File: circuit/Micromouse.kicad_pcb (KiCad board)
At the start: 2 copper layers, 0 parts

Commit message: スーパーエンジニアの登竜門たる文彦は当然スーパーエンジニア
あってぃ許さない
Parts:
- added C1: 4.7u, Capacitor_SMD:C_0805_2012Metric, F.Cu at (109.2, 58.4)
- added C10: 0.1u, Capacitor_SMD:C_0603_1608Metric, F.Cu at (102.6, 51.0)
- added C11: 0.1u, Capacitor_SMD:C_0603_1608Metric, F.Cu at (115.8, 38.6)
- added C12: 0.1u, Capacitor_SMD:C_0603_1608Metric, F.Cu at (106.6, 48.4)
- added C13: 0.1u, Capacitor_SMD:C_0603_1608Metric, F.Cu at (113.3, 41.3)
- added C14: 0.1u, Capacitor_SMD:C_0603_1608Metric, F.Cu at (119.8, 34.0)
- added C15: 1u, Capacitor_SMD:C_0603_1608Metric, F.Cu at (106.6, 51.0)
- added C17: 10u, Capacitor_SMD:C_0805_2012Metric, F.Cu at (44.0, 77.7)
- added C18: 47u, Capacitor_SMD:CP_Elec_6.3x7.7, F.Cu at (62.1, 72.9)
- added C19: 10u, Capacitor_SMD:C_0805_2012Metric, F.Cu at (39.5, 77.7)
- added C2: 0.1uF, Capacitor_SMD:C_0603_1608Metric, F.Cu at (87.6, 72.5)
- added C20: 10u, Capacitor_SMD:C_0805_2012Metric, F.Cu at (35.1, 77.7)
- added C21: 10u, Capacitor_SMD:C_0603_1608Metric, F.Cu at (72.4, 44.0)
- added C22: 10u, Capacitor_SMD:C_0603_1608Metric, F.Cu at (63.3, 51.5)
- added C23: 2.2u, Capacitor_SMD:C_0603_1608Metric, F.Cu at (110.6, 46.3)
- added C24: 2.2u, Capacitor_SMD:C_0603_1608Metric, F.Cu at (106.2, 70.1)
- added C3: 1u, Capacitor_SMD:C_0603_1608Metric, F.Cu at (102.2, 70.1)
- added C4: 2.2u, Capacitor_SMD:C_0603_1608Metric, F.Cu at (106.6, 67.2)
- added C5: 0.1u, Capacitor_SMD:C_0603_1608Metric, F.Cu at (119.8, 36.5)
- added C6: 2.2u, Capacitor_SMD:C_0603_1608Metric, F.Cu at (113.3, 43.8)
- added C7: 0.1u, Capacitor_SMD:C_0603_1608Metric, F.Cu at (83.5, 52.6)
- added C8: 0.1u, Capacitor_SMD:C_0603_1608Metric, F.Cu at (109.3, 43.6)
- added C9: 4.7u, Capacitor_SMD:C_0603_1608Metric, F.Cu at (115.8, 36.1)
- added CN1: Battery, Connector_JST:JST_PH_B2B-PH-K_1x02_P2.00mm_Vertical, F.Cu at (96.6, 59.6)
- added CN2: Battery, Connector_JST:JST_PH_B2B-PH-K_1x02_P2.00mm_Vertical, F.Cu at (95.2, 67.7)
- added D1: PWR_LED(Red), LED_SMD:LED_0603_1608Metric, F.Cu at (83.5, 72.5)
- added D2: TICK_LED, LED_SMD:LED_0603_1608Metric, F.Cu at (118.5, 31.4)
- added D3: DBG_LED0, LED_SMD:LED_0603_1608Metric, F.Cu at (111.8, 36.2)
- added D4: DBG_LED1, LED_SMD:LED_0603_1608Metric, F.Cu at (111.8, 38.8)
- added D5: DBG_LED2, LED_SMD:LED_0603_1608Metric, F.Cu at (102.6, 48.4)
- added D6: SFH4550, LED_THT:LED_D5.0mm_Horizontal_O3.81mm_Z9.0mm, F.Cu at (35.4, 31.9)
- added D7: SFH4550, LED_THT:LED_D5.0mm_Horizontal_O3.81mm_Z9.0mm, F.Cu at (42.9, 31.9)
- added D8: SFH4550, LED_THT:LED_D5.0mm_Horizontal_O3.81mm_Z9.0mm, F.Cu at (50.4, 31.9)
- added D9: SFH4550, LED_THT:LED_D5.0mm_Horizontal_O3.81mm_Z9.0mm, F.Cu at (57.9, 31.9)
- added J1: DBG_CN, Connector_PinSocket_2.54mm:PinSocket_1x03_P2.54mm_Vertical, F.Cu at (98.3, 44.7)
- added J2: ICM-20602_1-4pin, Connector_PinSocket_2.54mm:PinSocket_1x04_P2.54mm_Vertical, F.Cu at (102.9, 32.5)
- added J3: TEST_1P, TestPoint:TestPoint_Pad_D1.0mm, F.Cu at (114.2, 49.3)
- added J4: ICM-20602_5-8pin, Connector_PinSocket_2.54mm:PinSocket_1x04_P2.54mm_Vertical, F.Cu at (107.5, 32.5)
- added J5: TEST_1P, TestPoint:TestPoint_Pad_D1.0mm, F.Cu at (120.9, 41.8)
- added J6: Conn_01x04, Connector_PinSocket_2.54mm:PinSocket_1x04_P2.54mm_Vertical, F.Cu at (98.3, 32.5)
- added J7: Conn_02x03_Odd_Even, Connector_IDC:IDC-Header_2x03_P2.54mm_Vertical, F.Cu at (50.1, 64.9)
- added J8: Conn_02x03_Odd_Even, Connector_IDC:IDC-Header_2x03_P2.54mm_Vertical, F.Cu at (38.1, 64.9)
- added LS1: CSS-0575A-SMT, Original:CUI_CSS-0575A-SMT, F.Cu at (85.2, 48.0)
- added Q1: IRLML6402, Package_TO_SOT_SMD:SOT-23, F.Cu at (103.8, 63.6)
- added Q2: IRLML6344, Package_TO_SOT_SMD:SOT-23, F.Cu at (91.2, 51.6)
- added Q3: ST-1KL3A, LED_THT:LED_D5.0mm, F.Cu at (65.3, 41.5)
- added Q5: ST-1KL3A, LED_THT:LED_D5.0mm, F.Cu at (72.8, 33.9)
- added Q7: ST-1KL3A, LED_THT:LED_D5.0mm, F.Cu at (52.2, 49.0)
- added Q9: ST-1KL3A, LED_THT:LED_D5.0mm, F.Cu at (65.3, 33.9)
- added R1: 100k 0.25W, Resistor_SMD:R_0603_1608Metric, F.Cu at (108.1, 64.1)
- added R10: 10k, Resistor_SMD:R_0603_1608Metric, F.Cu at (119.8, 39.0)
- added R11: 10k, Resistor_SMD:R_0603_1608Metric, F.Cu at (34.9, 52.9)
- added R12: 1k, Resistor_SMD:R_0603_1608Metric, F.Cu at (38.9, 52.9)
- added R13: 10 1/10W, Resistor_SMD:R_0603_1608Metric, F.Cu at (42.9, 52.9)
- added R14: 24k, Resistor_SMD:R_0603_1608Metric, F.Cu at (46.9, 54.0)
- added R15: 1k, Resistor_SMD:R_0603_1608Metric, F.Cu at (59.3, 46.4)
- added R16: 10 1/10W, Resistor_SMD:R_0603_1608Metric, F.Cu at (50.9, 54.0)
- added R17: 1k, Resistor_SMD:R_0603_1608Metric, F.Cu at (72.4, 38.9)
- added R18: 24k, Resistor_SMD:R_0603_1608Metric, F.Cu at (54.9, 54.0)
- added R19: 10k, Resistor_SMD:R_0603_1608Metric, F.Cu at (59.3, 49.0)
- added R2: 20k, Resistor_SMD:R_0805_2012Metric, F.Cu at (102.4, 67.4)
- added R20: 1k, Resistor_SMD:R_0603_1608Metric, F.Cu at (59.3, 51.5)
- added R21: 24k, Resistor_SMD:R_0603_1608Metric, F.Cu at (63.3, 46.5)
- added R22: 10k, Resistor_SMD:R_0603_1608Metric, F.Cu at (72.4, 41.5)
- added R23: 10 1/10W, Resistor_SMD:R_0603_1608Metric, F.Cu at (67.3, 46.5)
- added R24: 10 1/10W, Resistor_SMD:R_0603_1608Metric, F.Cu at (63.3, 49.0)
- added R25: 24k, Resistor_SMD:R_0603_1608Metric, F.Cu at (59.3, 54.0)
- added R26: 10k, Resistor_SMD:R_0603_1608Metric, F.Cu at (76.4, 38.9)
- added R3: 10k, Resistor_SMD:R_0805_2012Metric, F.Cu at (109.2, 61.4)
- added R4: 1k, Resistor_SMD:R_0603_1608Metric, F.Cu at (102.2, 72.6)
- added R5: 10k, Resistor_SMD:R_0603_1608Metric, F.Cu at (114.6, 46.5)
- added R6: 10k, Resistor_SMD:R_0603_1608Metric, F.Cu at (110.6, 51.4)
- added R7: 10, Resistor_SMD:R_0603_1608Metric, F.Cu at (117.3, 44.0)
- added R8: 10k, Resistor_SMD:R_0603_1608Metric, F.Cu at (117.3, 41.5)
- added R9: 10k, Resistor_SMD:R_0603_1608Metric, F.Cu at (110.6, 48.9)
- added SW1: SW_SPDT, Button_Switch_THT:SW_CuK_JS202011CQN_DPDT_Straight, F.Cu at (84.5, 66.4)
- added SW2: SW_Push, Original:SW_TACT_ALPS_SKRPABE010, F.Cu at (113.1, 32.5)
- added SW3: SW_Push, Original:SW_TACT_ALPS_SKRPABE010, F.Cu at (92.3, 47.0)
- added SW4: SW_Push, Original:SW_TACT_ALPS_SKRPABE010, F.Cu at (103.9, 44.8)
- added U1: NJM7805S, Package_TO_SOT_SMD:TO-252-2, F.Cu at (87.6, 60.9)
- added U2: TB6612FNG, Package_SO:SSOP-24_5.3x8.2mm_P0.65mm, F.Cu at (62.1, 63.8)
- added U3: STM32F405RGTx, Package_QFP:LQFP-64_10x10mm_P0.5mm, F.Cu at (88.7, 37.4)
- added U4: ADP7182AUJZ-3.3, Package_TO_SOT_SMD:TSOT-23-5, F.Cu at (104.3, 59.1)
- added U5: AD8397, Package_SO:SOIC-8_3.9x4.9mm_P1.27mm, F.Cu at (37.1, 48.4)
- added U6: AD8397, Package_SO:SOIC-8_3.9x4.9mm_P1.27mm, F.Cu at (45.5, 48.4)
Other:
- board outline added: 268.6 x 181.3 mm

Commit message: AW何も分からん
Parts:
- removed J2: ICM-20602_1-4pin, Connector_PinSocket_2.54mm:PinSocket_1x04_P2.54mm_Vertical
- removed J4: ICM-20602_5-8pin, Connector_PinSocket_2.54mm:PinSocket_1x04_P2.54mm_Vertical
- removed J6: Conn_01x04, Connector_PinSocket_2.54mm:PinSocket_1x04_P2.54mm_Vertical
- removed the SW1 at (84.5, 66.4)
- removed SW2, SW3, SW4: SW_Push, Original:SW_TACT_ALPS_SKRPABE010
- added ICM-20602: ICM-20602-module, Original:ICM-20602, F.Cu at (190.0, 68.0)
- added RESET: SW_Push, Original:SW_TACT_ALPS_SKRPABE010, F.Cu at (154.5, 93.0)
- added SW0: SW_Push, Original:SW_TACT_ALPS_SKRPABE010, F.Cu at (205.0, 141.5)
- added SW1: SW_Push, Original:SW_TACT_ALPS_SKRPABE010, F.Cu at (209.5, 141.5)
- added SW1: SW_SPDT, Button_Switch_THT:SW_CuK_JS202011CQN_DPDT_Straight, F.Cu at (219.5, 93.5)
- added SWD: Conn_01x04, Connector_PinSocket_2.54mm:PinSocket_1x04_P2.54mm_Vertical, F.Cu at (153.0, 97.5)
- D8, D9: footprint LED_THT:LED_D5.0mm_Horizontal_O3.81mm_Z9.0mm -> Original:LED_D5.0mm_Horizontal_O3.81mm_Z9.0mm_reverse
- Q3, Q5, Q7, Q9: footprint LED_THT:LED_D5.0mm -> Original:ST-1KL3A_ForWall
- moved D6 199.7 mm to (227.0, 88.0), turned to 180 degrees
- moved J8 195.7 mm to (218.3, 141.3), turned to 90 degrees
- moved U5 171.0 mm to (207.0, 68.0), turned to 180 degrees
- moved Q3 167.6 mm to (227.0, 85.6), turned to 180 degrees
- moved D7 164.1 mm to (204.5, 60.4), turned to 105 degrees
- moved C18 144.5 mm to (190.0, 140.0)
- moved U2 143.1 mm to (190.0, 128.0), turned to 90 degrees
- moved Q5 136.3 mm to (206.7, 59.8), turned to 105 degrees
- moved J7 131.1 mm to (156.6, 141.3), turned to 90 degrees
- moved U6 128.9 mm to (173.0, 68.0), turned to 180 degrees
- moved D8 128.4 mm to (175.5, 60.4), turned to 255 degrees
- moved J1 122.5 mm to (171.5, 143.0), turned to 90 degrees
- moved Q7 121.5 mm to (173.3, 59.8), turned to 255 degrees
- moved CN2 121.2 mm to (212.0, 100.0), turned to 270 degrees
- moved CN1 120.1 mm to (212.0, 93.0), turned to 270 degrees
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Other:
- board size 268.6 x 181.3 mm -> 78 x 100 mm
- board text added: "G"
- board text added: "GND"
- board text added: "NRST"
- board text added: "RX"
- board text added: "SWCLK"
- board text added: "SWDIO"
- board text added: "TX"
- board text added: "→"

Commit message: ぽんぽんぺいん
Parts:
- moved D3 137.4 mm to (198.2, 143.0), turned to 90 degrees
- moved D5 137.1 mm to (201.9, 143.0), turned to 90 degrees
- moved D4 136.5 mm to (200.0, 143.0), turned to 90 degrees
- moved D1 134.1 mm to (215.7, 95.5), turned to 90 degrees
- moved D2 77.9 mm to (164.0, 94.7), turned to 90 degrees
- moved J1 0.12 mm to (171.4, 142.9)
- renumbered SWD to J6, RESET to SW2, SW0 to SW3, SW1 to SW4, ICM-20602 to U7
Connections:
- D2 pad 1: Net-(D2-Pad1) -> GND
- D2 pad 2: /TICK_LED -> Net-(D2-Pad2)
- D3 pad 1: Net-(D3-Pad1) -> GND
- D3 pad 2: /DBG_LED0 -> Net-(D3-Pad2)
- D4 pad 1: Net-(D4-Pad1) -> GND
- D4 pad 2: /DBG_LED1 -> Net-(D4-Pad2)
- D5 pad 1: Net-(D5-Pad1) -> GND
- D5 pad 2: /DBG_LED2 -> Net-(D5-Pad2)
- R10 pad 1: Net-(D5-Pad1) -> /DBG_LED2
- R10 pad 2: GND -> Net-(D5-Pad2)
- R5 pad 1: Net-(D2-Pad1) -> /TICK_LED
- R5 pad 2: GND -> Net-(D2-Pad2)
- R6 pad 1: Net-(D3-Pad1) -> /DBG_LED0
- R6 pad 2: GND -> Net-(D3-Pad2)
- R9 pad 1: Net-(D4-Pad1) -> /DBG_LED1
- R9 pad 2: GND -> Net-(D4-Pad2)

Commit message: 何となーくの部品配置
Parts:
- moved R12 139.9 mm to (175.6, 82.4), turned to 90 degrees
- moved R11 132.4 mm to (166.8, 64.3), turned to 90 degrees
- moved R13 128.7 mm to (170.6, 68.7), turned to 270 degrees
- moved R14 122.4 mm to (168.7, 66.0), turned to 90 degrees
- moved C20 120.9 mm to (153.0, 104.3)
- moved C19 116.0 mm to (153.2, 100.8)
- moved R16 111.2 mm to (161.8, 61.9)
- moved C17 106.6 mm to (143.5, 115.8), turned to 180 degrees
- moved C8 106.2 mm to (164.7, 134.2), turned to 180 degrees
- moved C5 105.7 mm to (160.0, 134.3), turned to 180 degrees
- moved R10 104.5 mm to (156.6, 136.8), turned to 270 degrees
- moved C21 103.9 mm to (152.6, 110.0)
- moved R18 101.6 mm to (156.1, 63.8)
- moved R9 98.4 mm to (154.7, 136.8), turned to 270 degrees
- moved R19 98.4 mm to (156.1, 66.3), turned to 270 degrees
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- renumbered D3 to LED0, D4 to LED1, D5 to LED2

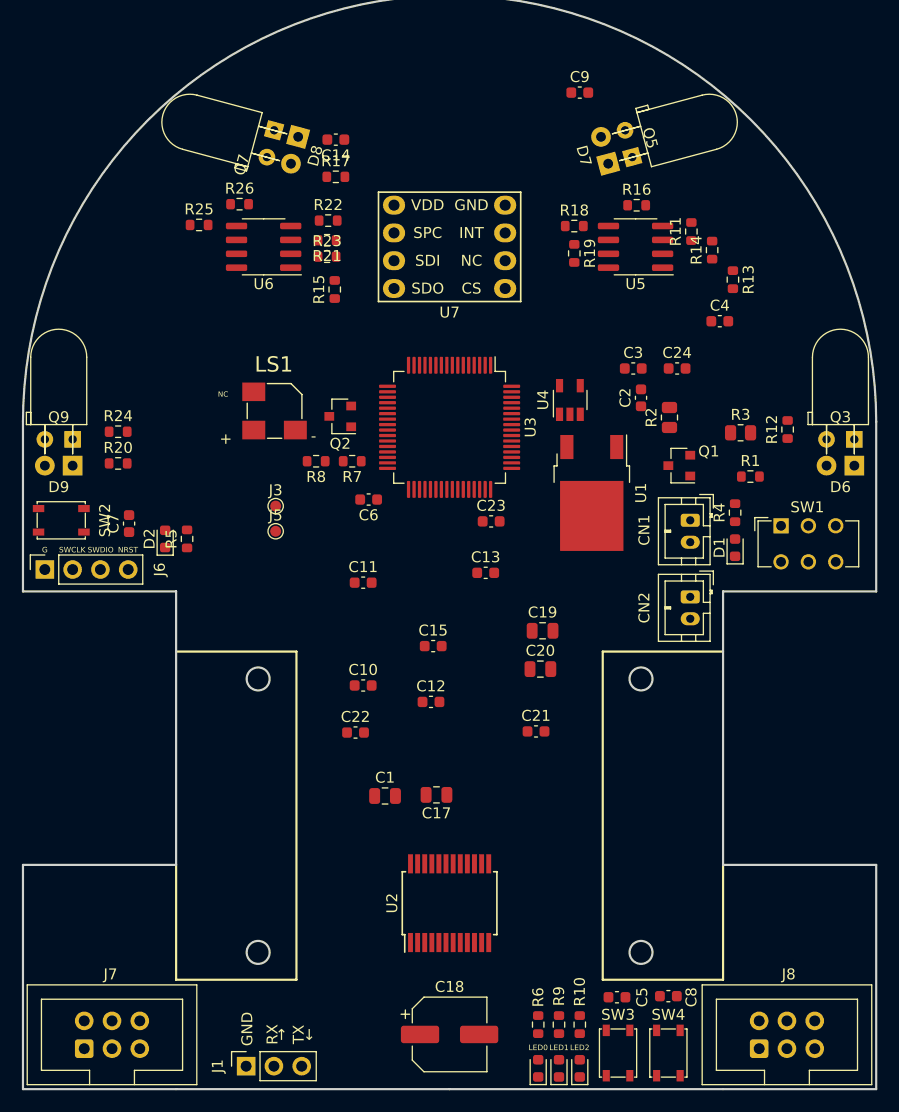
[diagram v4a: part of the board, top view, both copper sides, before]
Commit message: 配置大体完了．配線分からん
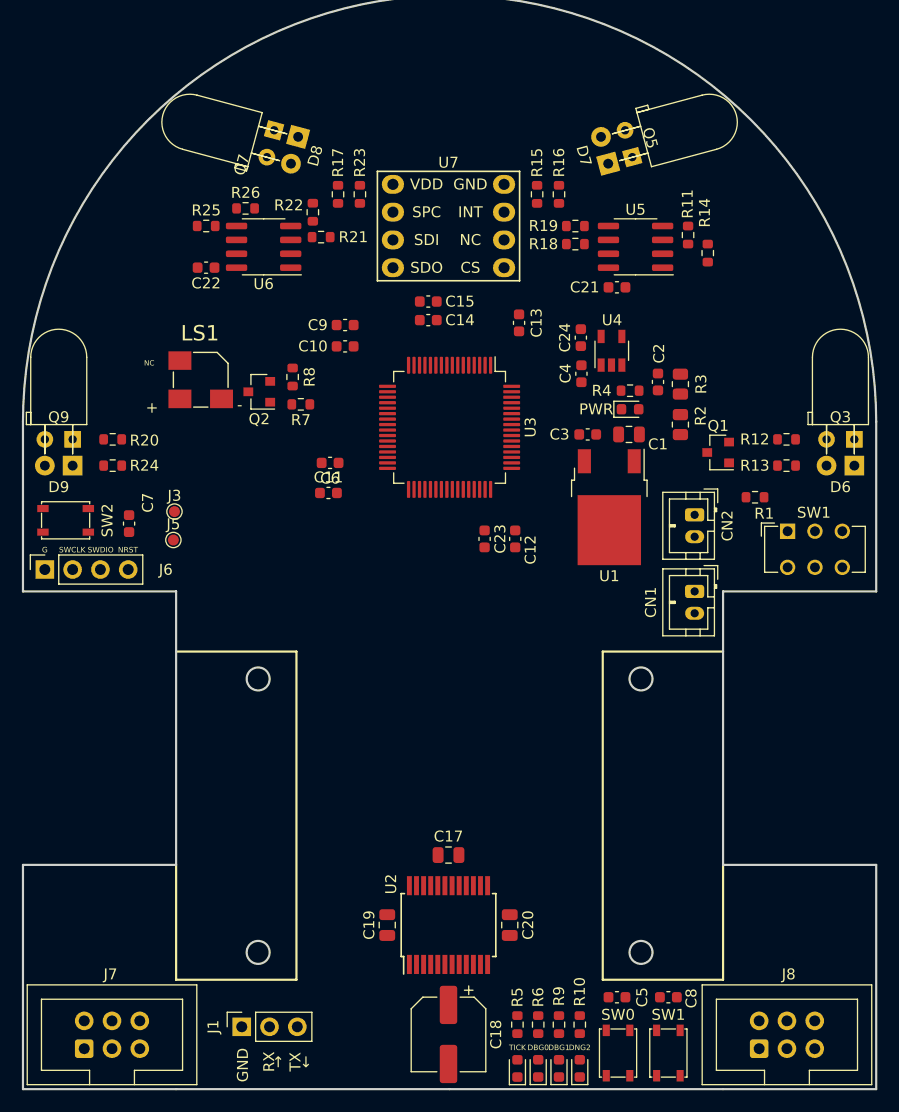
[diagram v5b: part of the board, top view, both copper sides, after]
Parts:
- removed D1: PWR_LED(Red), LED_SMD:LED_0603_1608Metric
- removed D2: TICK_LED, LED_SMD:LED_0603_1608Metric
- added PWR: PWR_LED(Red), LED_SMD:LED_0603_1608Metric, F.Cu at (161.2, 80.5)
- added TICK: TICK_LED, LED_SMD:LED_0603_1608Metric, F.Cu at (150.9, 140.8)
- moved R5 53.7 mm to (150.9, 136.8), turned to 270 degrees
- moved C22 44.6 mm to (122.4, 67.6), turned to 180 degrees
- moved C21 41.3 mm to (160.0, 69.4)
- moved C1 39.9 mm to (161.1, 82.8), turned to 180 degrees
- moved C15 31.5 mm to (142.8, 70.7), turned to 180 degrees
- moved C10 31.0 mm to (135.2, 74.8), turned to 180 degrees
- moved C19 30.4 mm to (139.0, 127.7), turned to 270 degrees
- moved C9 30.2 mm to (135.2, 72.8), turned to 180 degrees
- moved C20 23.6 mm to (150.2, 127.7), turned to 270 degrees
- moved C13 23.1 mm to (151.1, 72.7), turned to 90 degrees
- moved R15 20.4 mm to (152.7, 60.9), turned to 270 degrees
- moved C14 18.5 mm to (142.8, 72.4)
- moved R13 17.7 mm to (175.5, 85.7), turned to 180 degrees
- moved C12 16.8 mm to (150.7, 92.4), turned to 270 degrees
- moved R4 14.7 mm to (161.2, 78.8), turned to 0 degrees
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- renumbered LED0 to DBG0, LED1 to DBG1, LED2 to DNG2, SW3 to SW0, SW4 to SW1

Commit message: 1A＝1ｍｍ・・・結構大変
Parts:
- moved R3 1.78 mm to (166.2, 80.0)
- moved C2 1.77 mm to (164.2, 79.8)
- moved R2 1.68 mm to (166.2, 83.6)
- moved C18 1.27 mm to (144.6, 139.0), turned to 0 degrees
- moved R1 1.12 mm to (173.4, 89.4)
- moved CN1 0.72 mm to (166.4, 97.3)
- moved CN2 0.70 mm to (166.4, 90.2)
- moved U4 0.61 mm to (159.2, 74.7)
- moved C1 0.53 mm to (160.6, 82.6)
- moved J1 0.43 mm to (125.7, 137.4)
- moved C15 0.40 mm to (142.8, 71.1)
- moved C5 0.40 mm to (160.0, 134.7)
- moved C8 0.40 mm to (164.7, 134.7)
- moved SW0 0.30 mm to (160.1, 139.7)
- moved C14 0.30 mm to (142.8, 72.7)
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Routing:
- net +5V: track 0.00 -> 151.8 mm, vias 0 -> 2
- net VCC: track 0.00 -> 120.7 mm
- net /Motor/MOTOR_L+: track 0.00 -> 43.8 mm, vias 0 -> 2
- net /Motor/MOTOR_R+: track 0.00 -> 42.8 mm
- net /Motor/MOTOR_L-: track 0.00 -> 42.0 mm, vias 0 -> 2
- net /Motor/MOTOR_R-: track 0.00 -> 37.1 mm
- net +BATT: track 0.00 -> 23.0 mm
- net GND: track 0.00 -> 7.40 mm
- net Net-(R1-Pad2): track 0.00 -> 6.03 mm
- net Net-(CN1-Pad1): track 0.00 -> 5.15 mm
- net Net-(D1-Pad2): track 0.00 -> 1.72 mm

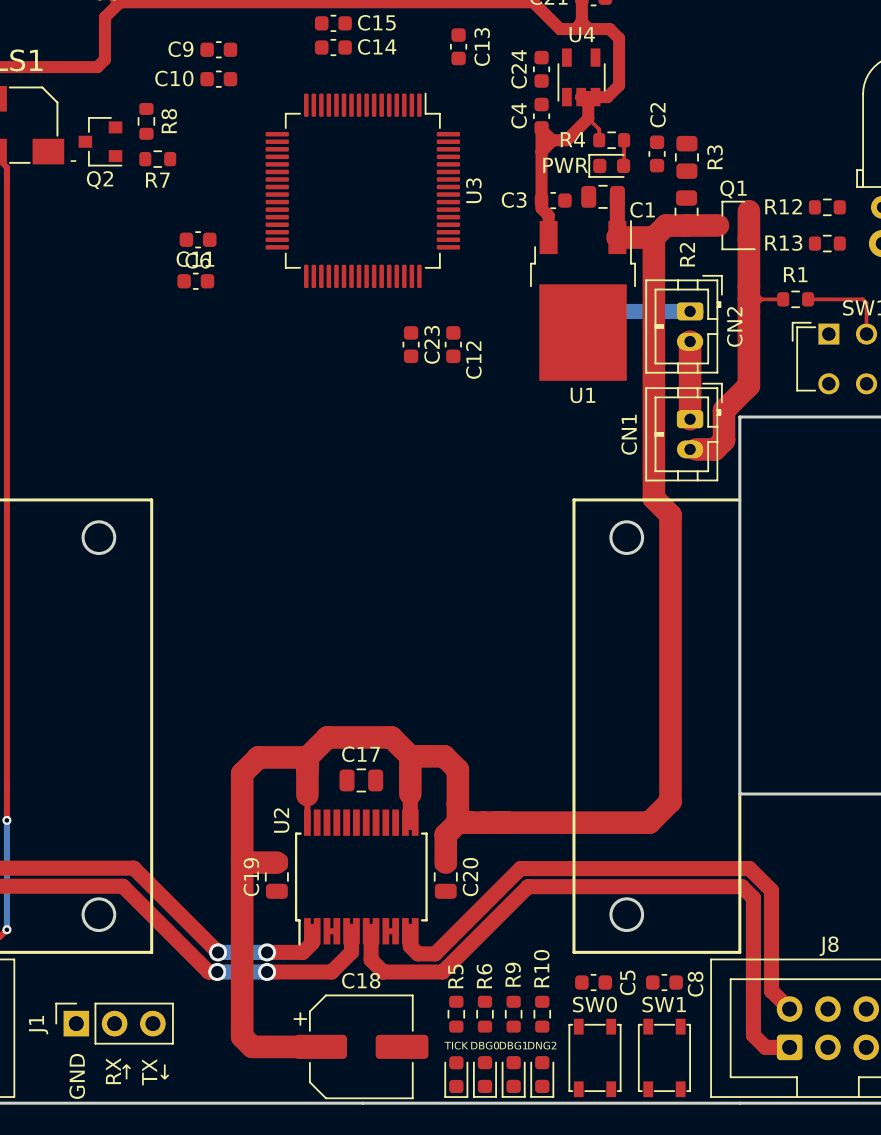
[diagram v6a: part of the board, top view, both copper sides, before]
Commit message: ベタ配線のやり方ちょっとわかってきた
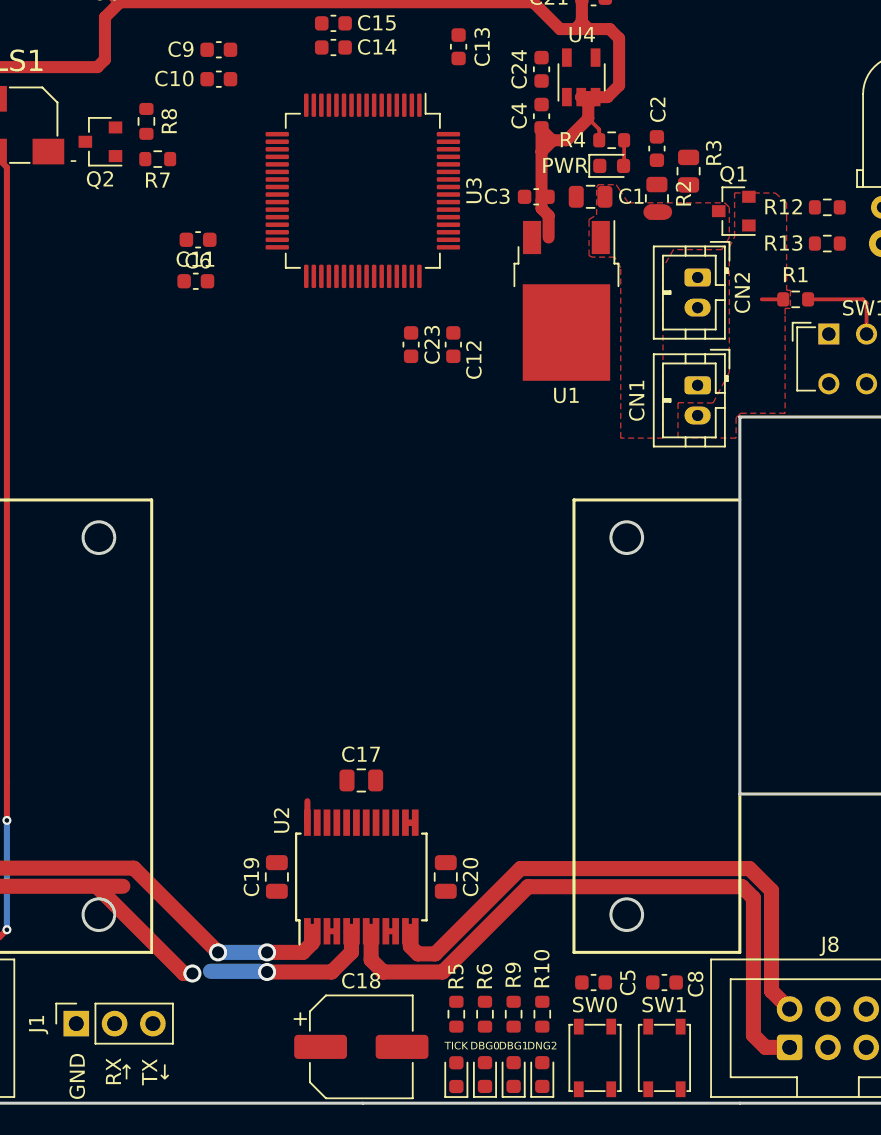
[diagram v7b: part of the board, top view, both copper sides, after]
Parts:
- moved CN1 2.30 mm to (166.9, 95.1)
- moved CN2 2.30 mm to (166.9, 88.0)
- moved R2 2.16 mm to (164.2, 82.7)
- moved C3 1.15 mm to (156.2, 82.6)
- moved U1 1.10 mm to (158.2, 89.5)
- moved Q1 0.95 mm to (169.3, 83.5)
- moved R3 0.92 mm to (166.3, 80.9)
- moved C1 0.83 mm to (159.8, 82.6)
- moved C2 0.36 mm to (164.2, 79.4)
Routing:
- net VCC: track 120.7 -> 2.99 mm
- net +BATT: track 23.0 -> 1.42 mm
- net GND: track 7.40 -> 1.30 mm
- net Net-(CN1-Pad1): track 5.15 -> 0.00 mm
- added copper zone on F.Cu, net +BATT
- added copper zone on F.Cu, net VCC
